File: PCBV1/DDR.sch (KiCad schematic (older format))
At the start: 24 parts, among them U2 MT41K128M16JT-125_K

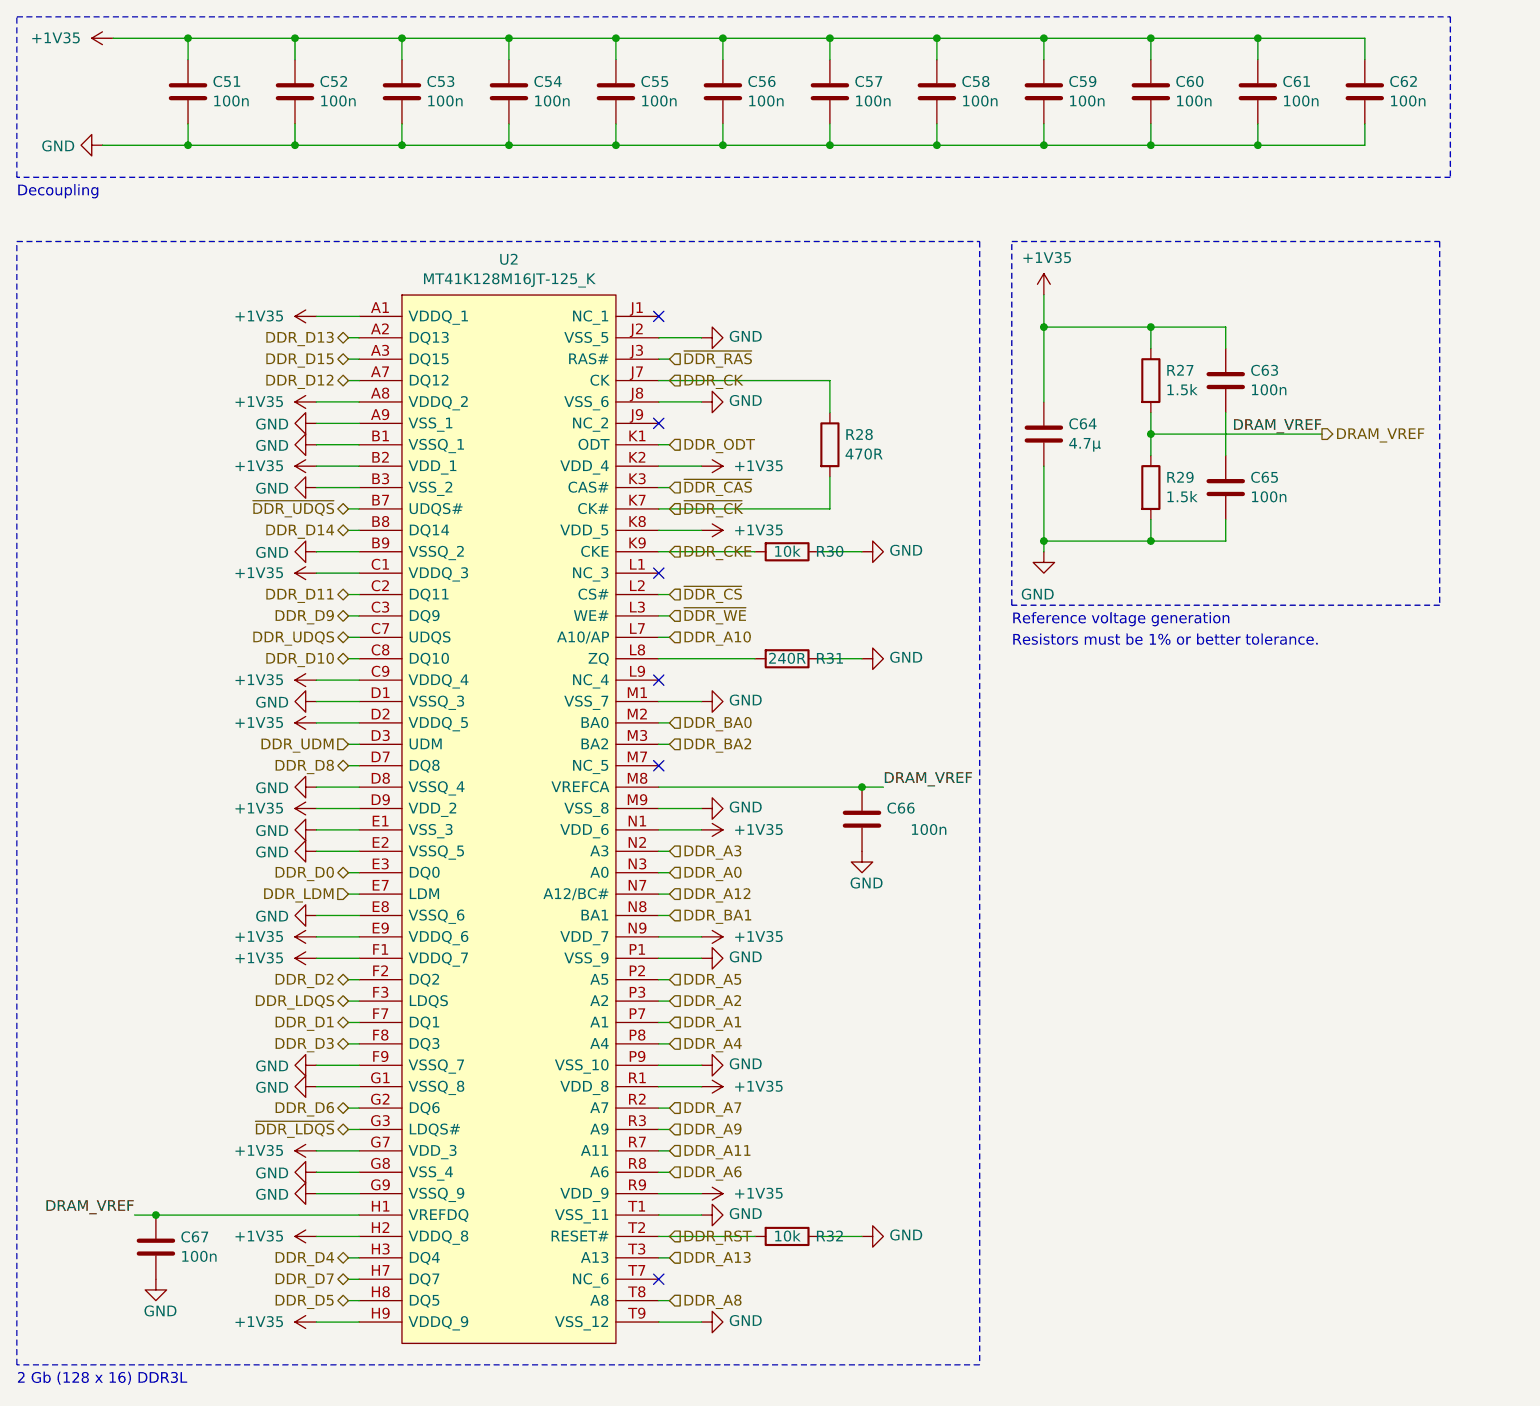
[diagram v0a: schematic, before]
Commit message: Many changes to footprints (0603 -> 0402), basic DDR layout set, no traces made.
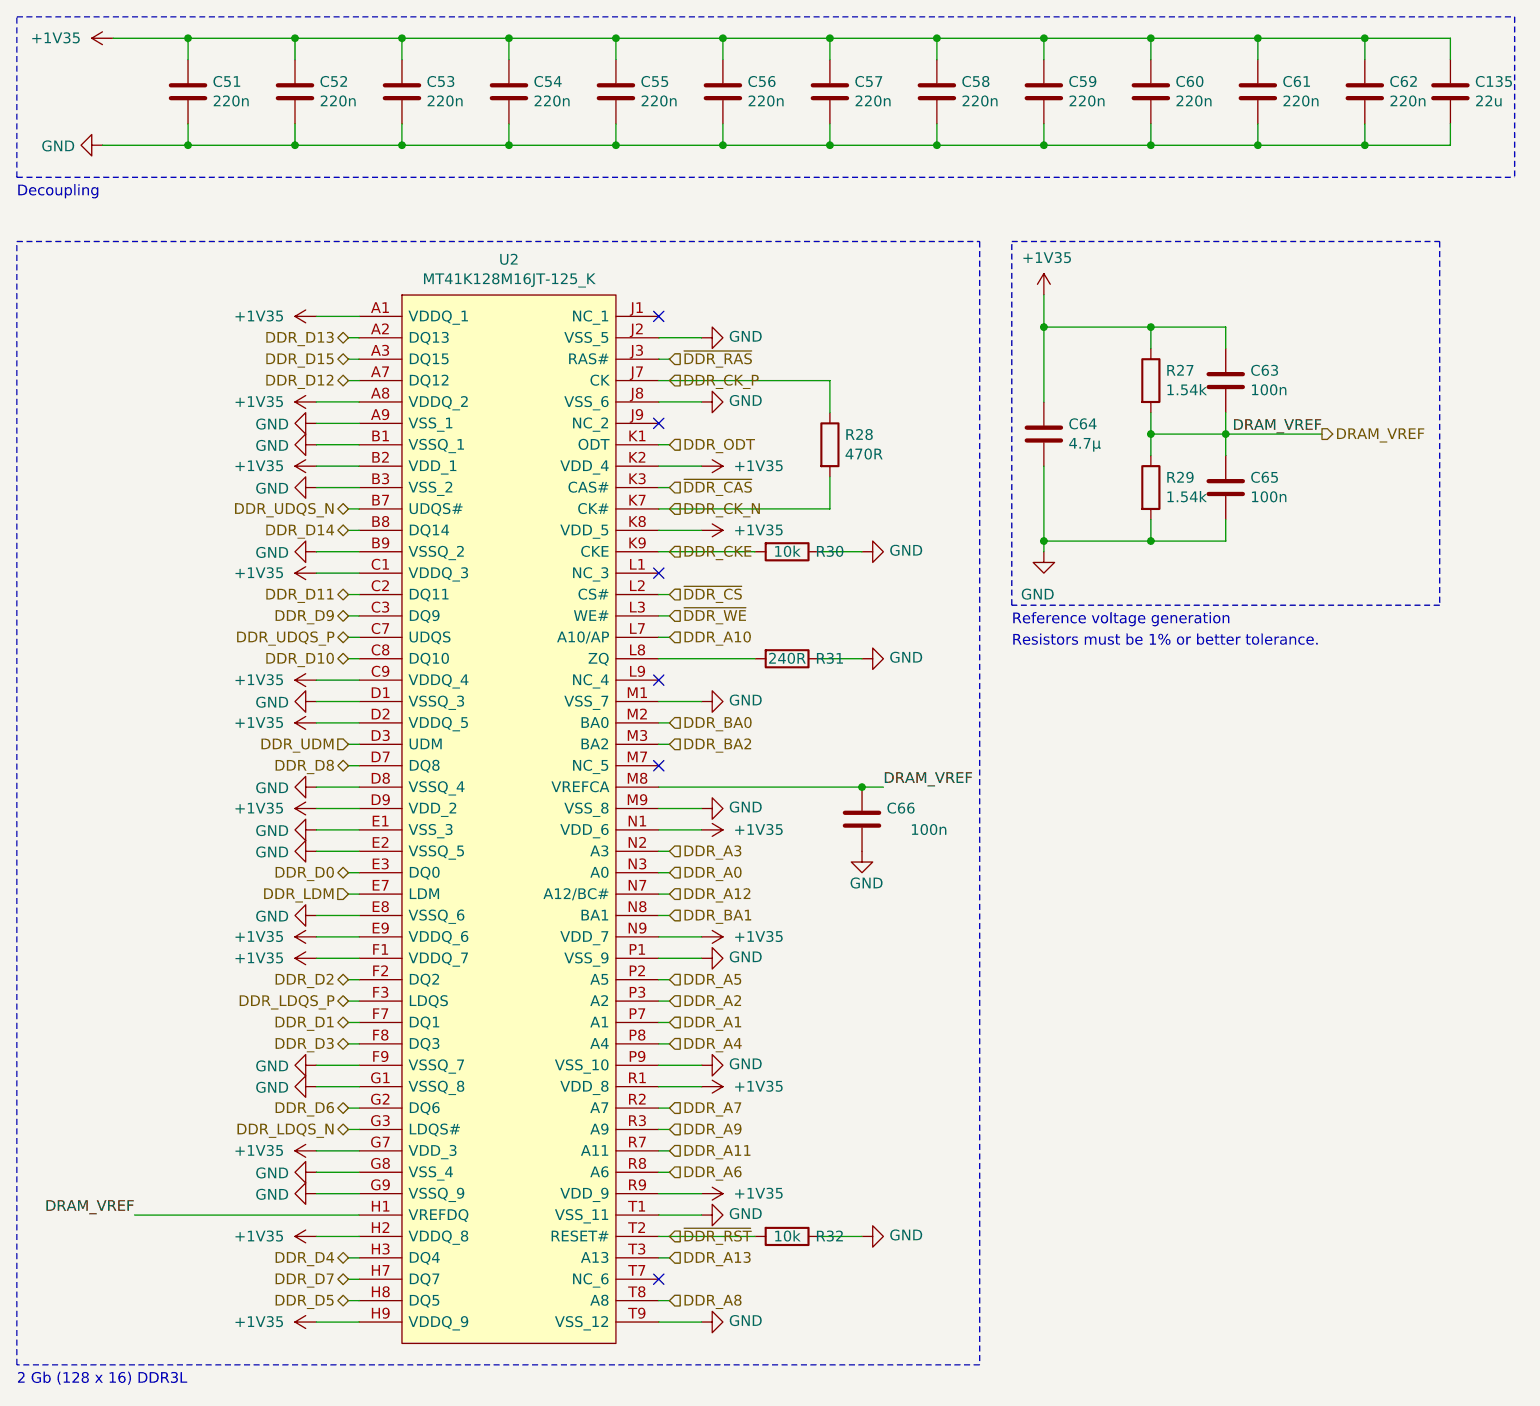
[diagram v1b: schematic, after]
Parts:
- removed C67: 100n, Capacitor_SMD:C_0603_1608Metric, symbol Device:C
- added C135: 22u, Capacitor_SMD:C_0603_1608Metric, symbol Device:C
- C51, C52, C53, C54, C55, C56, C57, C58, C59, C60, C61, C62: value 100n -> 220n; footprint Capacitor_SMD:C_0603_1608Metric -> Capacitor_SMD:C_0402_1005Metric
- C63, C65, C66: footprint Capacitor_SMD:C_0603_1608Metric -> Capacitor_SMD:C_0402_1005Metric
- R27, R29: value 1.5k -> 1.54k; footprint Resistor_SMD:R_0603_1608Metric -> Resistor_SMD:R_0402_1005Metric
- R28, R30, R31, R32: footprint Resistor_SMD:R_0603_1608Metric -> Resistor_SMD:R_0402_1005Metric
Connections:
- net +1V35: now also C135.1
- net DRAM_VREF: now also C63.2, C65.1
- net GND: now also C135.2
- net DDR_CK renamed DDR_CK_P
- net DDR_LDQS renamed DDR_LDQS_P
- net DDR_RST renamed ~DDR_RST
- net DDR_UDQS renamed DDR_UDQS_P
- net ~DDR_CK renamed DDR_CK_N
- net ~DDR_LDQS renamed DDR_LDQS_N
- net ~DDR_UDQS renamed DDR_UDQS_N
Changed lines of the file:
@@
 F 0 "R31" V 4150 3800 50  0000 C CNN
 F 1 "240R" V 4150 3600 50  0000 C CNN
-F 2 "Resistor_SMD:R_0603_1608Metric" V 4080 3600 50  0001 C CNN
+F 2 "Resistor_SMD:R_0402_1005Metric" V 4080 3600 50  0001 C CNN
 F 3 "~" H 4150 3600 50  0001 C CNN
 	1    4150 3600
@@
 DDR_CKE
 Text HLabel 3600 2900 2    50   Input ~ 0
-~DDR_CK
+DDR_CK_N
 Text HLabel 3600 2800 2    50   Input ~ 0
 ~DDR_CAS
@@
 	3550 2800 3600 2800
 Text HLabel 3600 2300 2    50   Input ~ 0
-DDR_CK
+DDR_CK_P
 Text HLabel 3600 2200 2    50   Input ~ 0
 ~DDR_RAS
@@
 	3550 2200 3600 2200
 Text HLabel 2100 2900 0    50   BiDi ~ 0
-~DDR_UDQS
+DDR_UDQS_N
 Wire Wire Line
 	2100 2900 2150 2900
 Text HLabel 2100 3500 0    50   BiDi ~ 0
-DDR_UDQS
+DDR_UDQS_P
 Wire Wire Line
 	2100 3500 2150 3500
@@
 	2100 4700 2150 4700
 Text HLabel 2100 5200 0    50   BiDi ~ 0
-DDR_LDQS
+DDR_LDQS_P
 Wire Wire Line
 	2100 5200 2150 5200
 Text HLabel 2100 5800 0    50   BiDi ~ 0
-~DDR_LDQS
+DDR_LDQS_N
 Wire Wire Line
 	2100 5800 2150 5800
@@
 	3750 6100 3550 6100
 Text HLabel 3600 6300 2    50   Input ~ 0
-DDR_RST
+~DDR_RST
 $Comp
 L power:+1V35 #PWR0120
@@
 P 1350 950
 F 0 "C51" H 1465 996 50  0000 L CNN
-F 1 "100n" H 1465 905 50  0000 L CNN
-F 2 "Capacitor_SMD:C_0603_1608Metric" H 1388 800 50  0001 C CNN
+F 1 "220n" H 1465 905 50  0000 L CNN
+F 2 "Capacitor_SMD:C_0402_1005Metric" H 1388 800 50  0001 C CNN
 F 3 "~" H 1350 950 50  0001 C CNN
 	1    1350 950
@@
 P 1850 950
 F 0 "C52" H 1965 996 50  0000 L CNN
-F 1 "100n" H 1965 905 50  0000 L CNN
-F 2 "Capacitor_SMD:C_0603_1608Metric" H 1888 800 50  0001 C CNN
+F 1 "220n" H 1965 905 50  0000 L CNN
+F 2 "Capacitor_SMD:C_0402_1005Metric" H 1888 800 50  0001 C CNN
 F 3 "~" H 1850 950 50  0001 C CNN
 	1    1850 950
@@
 P 2350 950
 F 0 "C53" H 2465 996 50  0000 L CNN
-F 1 "100n" H 2465 905 50  0000 L CNN
-F 2 "Capacitor_SMD:C_0603_1608Metric" H 2388 800 50  0001 C CNN
+F 1 "220n" H 2465 905 50  0000 L CNN
+F 2 "Capacitor_SMD:C_0402_1005Metric" H 2388 800 50  0001 C CNN
 F 3 "~" H 2350 950 50  0001 C CNN
 	1    2350 950
@@
 P 2850 950
 F 0 "C54" H 2965 996 50  0000 L CNN
-F 1 "100n" H 2965 905 50  0000 L CNN
-F 2 "Capacitor_SMD:C_0603_1608Metric" H 2888 800 50  0001 C CNN
+F 1 "220n" H 2965 905 50  0000 L CNN
+F 2 "Capacitor_SMD:C_0402_1005Metric" H 2888 800 50  0001 C CNN
 F 3 "~" H 2850 950 50  0001 C CNN
 	1    2850 950
@@
 P 3350 950
 F 0 "C55" H 3465 996 50  0000 L CNN
-F 1 "100n" H 3465 905 50  0000 L CNN
-F 2 "Capacitor_SMD:C_0603_1608Metric" H 3388 800 50  0001 C CNN
+F 1 "220n" H 3465 905 50  0000 L CNN
+F 2 "Capacitor_SMD:C_0402_1005Metric" H 3388 800 50  0001 C CNN
 F 3 "~" H 3350 950 50  0001 C CNN
 	1    3350 950
@@
 P 3850 950
 F 0 "C56" H 3965 996 50  0000 L CNN
-F 1 "100n" H 3965 905 50  0000 L CNN
-F 2 "Capacitor_SMD:C_0603_1608Metric" H 3888 800 50  0001 C CNN
+F 1 "220n" H 3965 905 50  0000 L CNN
+F 2 "Capacitor_SMD:C_0402_1005Metric" H 3888 800 50  0001 C CNN
 F 3 "~" H 3850 950 50  0001 C CNN
 	1    3850 950
@@
 P 4350 950
 F 0 "C57" H 4465 996 50  0000 L CNN
-F 1 "100n" H 4465 905 50  0000 L CNN
-F 2 "Capacitor_SMD:C_0603_1608Metric" H 4388 800 50  0001 C CNN
+F 1 "220n" H 4465 905 50  0000 L CNN
+F 2 "Capacitor_SMD:C_0402_1005Metric" H 4388 800 50  0001 C CNN
 F 3 "~" H 4350 950 50  0001 C CNN
 	1    4350 950
@@
 P 4850 950
 F 0 "C58" H 4965 996 50  0000 L CNN
-F 1 "100n" H 4965 905 50  0000 L CNN
-F 2 "Capacitor_SMD:C_0603_1608Metric" H 4888 800 50  0001 C CNN
+F 1 "220n" H 4965 905 50  0000 L CNN
+F 2 "Capacitor_SMD:C_0402_1005Metric" H 4888 800 50  0001 C CNN
 F 3 "~" H 4850 950 50  0001 C CNN
 	1    4850 950
@@
 P 5350 950
 F 0 "C59" H 5465 996 50  0000 L CNN
-F 1 "100n" H 5465 905 50  0000 L CNN
-F 2 "Capacitor_SMD:C_0603_1608Metric" H 5388 800 50  0001 C CNN
+F 1 "220n" H 5465 905 50  0000 L CNN
+F 2 "Capacitor_SMD:C_0402_1005Metric" H 5388 800 50  0001 C CNN
 F 3 "~" H 5350 950 50  0001 C CNN
 	1    5350 950
@@
 P 5850 950
 F 0 "C60" H 5965 996 50  0000 L CNN
-F 1 "100n" H 5965 905 50  0000 L CNN
-F 2 "Capacitor_SMD:C_0603_1608Metric" H 5888 800 50  0001 C CNN
+F 1 "220n" H 5965 905 50  0000 L CNN
+F 2 "Capacitor_SMD:C_0402_1005Metric" H 5888 800 50  0001 C CNN
 F 3 "~" H 5850 950 50  0001 C CNN
 	1    5850 950
@@
 P 6350 950
 F 0 "C61" H 6465 996 50  0000 L CNN
-F 1 "100n" H 6465 905 50  0000 L CNN
-F 2 "Capacitor_SMD:C_0603_1608Metric" H 6388 800 50  0001 C CNN
+F 1 "220n" H 6465 905 50  0000 L CNN
+F 2 "Capacitor_SMD:C_0402_1005Metric" H 6388 800 50  0001 C CNN
 F 3 "~" H 6350 950 50  0001 C CNN
 	1    6350 950
@@
 P 6850 950
 F 0 "C62" H 6965 996 50  0000 L CNN
-F 1 "100n" H 6965 905 50  0000 L CNN
-F 2 "Capacitor_SMD:C_0603_1608Metric" H 6888 800 50  0001 C CNN
+F 1 "220n" H 6965 905 50  0000 L CNN
+F 2 "Capacitor_SMD:C_0402_1005Metric" H 6888 800 50  0001 C CNN
 F 3 "~" H 6850 950 50  0001 C CNN
 	1    6850 950
@@
 P 5850 2300
 F 0 "R27" H 5920 2346 50  0000 L CNN
-F 1 "1.5k" H 5920 2255 50  0000 L CNN
-F 2 "Resistor_SMD:R_0603_1608Metric" V 5780 2300 50  0001 C CNN
+F 1 "1.54k" H 5920 2255 50  0000 L CNN
+F 2 "Resistor_SMD:R_0402_1005Metric" V 5780 2300 50  0001 C CNN
 F 3 "~" H 5850 2300 50  0001 C CNN
 	1    5850 2300
@@
 P 5850 2800
 F 0 "R29" H 5920 2846 50  0000 L CNN
-F 1 "1.5k" H 5920 2755 50  0000 L CNN
-F 2 "Resistor_SMD:R_0603_1608Metric" V 5780 2800 50  0001 C CNN
+F 1 "1.54k" H 5920 2755 50  0000 L CNN
+F 2 "Resistor_SMD:R_0402_1005Metric" V 5780 2800 50  0001 C CNN
 F 3 "~" H 5850 2800 50  0001 C CNN
 	1    5850 2800
@@
 F 0 "C63" H 6315 2346 50  0000 L CNN
 F 1 "100n" H 6315 2255 50  0000 L CNN
-F 2 "Capacitor_SMD:C_0603_1608Metric" H 6238 2150 50  0001 C CNN
+F 2 "Capacitor_SMD:C_0402_1005Metric" H 6238 2150 50  0001 C CNN
 F 3 "~" H 6200 2300 50  0001 C CNN
 	1    6200 2300
@@
 F 0 "C65" H 6315 2846 50  0000 L CNN
 F 1 "100n" H 6315 2755 50  0000 L CNN
-F 2 "Capacitor_SMD:C_0603_1608Metric" H 6238 2650 50  0001 C CNN
+F 2 "Capacitor_SMD:C_0402_1005Metric" H 6238 2650 50  0001 C CNN
 F 3 "~" H 6200 2800 50  0001 C CNN
 	1    6200 2800
@@
 Connection ~ 5850 2050
 Wire Wire Line
-	6200 2450 6200 2650
-Wire Wire Line
-	5850 2450 5850 2550
-Connection ~ 5850 2550
-Wire Wire Line
-	5850 2550 5850 2650
+	6200 2450 6200 2550
 Text Label 6650 2550 2    50   ~ 0
 DRAM_VREF
-Wire Wire Line
-	5850 2550 6650 2550
 Text HLabel 6650 2550 2    50   Output ~ 0
 DRAM_VREF
@@
 Text Label 1100 6200 2    50   ~ 0
 DRAM_VREF
-$Comp
-L Device:C C67
-U 1 1 6049FFC4
-P 1200 6350
-F 0 "C67" H 1315 6396 50  0000 L CNN
-F 1 "100n" H 1315 6305 50  0000 L CNN
-F 2 "Capacitor_SMD:C_0603_1608Metric" H 1238 6200 50  0001 C CNN
-F 3 "~" H 1200 6350 50  0001 C CNN
-	1    1200 6350
-	1    0    0    -1
-$EndComp
-Wire Wire Line
-	1100 6200 1200 6200
-Connection ~ 1200 6200
-Wire Wire Line
-	1200 6200 2150 6200
 Text Label 4600 4200 0    50   ~ 0
 DRAM_VREF
@@
 F 0 "C66" H 4250 4300 50  0000 L CNN
 F 1 "100n" H 4100 4400 50  0000 L CNN
-F 2 "Capacitor_SMD:C_0603_1608Metric" H 4538 4200 50  0001 C CNN
+F 2 "Capacitor_SMD:C_0402_1005Metric" H 4538 4200 50  0001 C CNN
 F 3 "~" H 4500 4350 50  0001 C CNN
 	1    4500 4350
@@
 	1    0    0    -1
 $EndComp
-$Comp
-L power:GND #PWR0128
-U 1 1 604B3DEB
-P 1200 6500
-F 0 "#PWR0128" H 1200 6250 50  0001 C CNN
-F 1 "GND" H 1300 6350 50  0000 R CNN
-F 2 "" H 1200 6500 50  0001 C CNN
-F 3 "" H 1200 6500 50  0001 C CNN
-	1    1200 6500
-	1    0    0    -1
-$EndComp
 Wire Notes Line
 	550  6900 550  1650
@@
 Text Notes 550  7000 0    50   ~ 0
 2 Gb (128 x 16) DDR3L
-Wire Notes Line
-	550  600  7250 600
-Wire Notes Line
-	7250 600  7250 1350
-Wire Notes Line
-	7250 1350 550  1350
 Wire Notes Line
 	550  1350 550  600
@@
 F 0 "R32" V 4150 6500 50  0000 C CNN
 F 1 "10k" V 4150 6300 50  0000 C CNN
-F 2 "Resistor_SMD:R_0603_1608Metric" V 4080 6300 50  0001 C CNN
+F 2 "Resistor_SMD:R_0402_1005Metric" V 4080 6300 50  0001 C CNN
 F 3 "~" H 4150 6300 50  0001 C CNN
 	1    4150 6300
@@
 F 0 "R30" V 4150 3300 50  0000 C CNN
 F 1 "10k" V 4150 3100 50  0000 C CNN
-F 2 "Resistor_SMD:R_0603_1608Metric" V 4080 3100 50  0001 C CNN
+F 2 "Resistor_SMD:R_0402_1005Metric" V 4080 3100 50  0001 C CNN
 F 3 "~" H 4150 3100 50  0001 C CNN
 	1    4150 3100
@@
 F 0 "R28" H 4420 2646 50  0000 L CNN
 F 1 "470R" H 4420 2555 50  0000 L CNN
-F 2 "Resistor_SMD:R_0603_1608Metric" V 4280 2600 50  0001 C CNN
+F 2 "Resistor_SMD:R_0402_1005Metric" V 4280 2600 50  0001 C CNN
 F 3 "~" H 4350 2600 50  0001 C CNN
 	1    4350 2600
@@
 Wire Wire Line
 	4350 2750 4350 2900
+Wire Wire Line
+	5850 2450 5850 2550
+Wire Wire Line
+	5850 2550 6200 2550
+Connection ~ 5850 2550
+Wire Wire Line
+	5850 2550 5850 2650
+Connection ~ 6200 2550
+Wire Wire Line
+	6200 2550 6200 2650
+Wire Wire Line
+	6200 2550 6650 2550
+$Comp
+L Device:C C135
+U 1 1 628AE7E6
+P 7250 950
+F 0 "C135" H 7365 996 50  0000 L CNN
+F 1 "22u" H 7365 905 50  0000 L CNN
+F 2 "Capacitor_SMD:C_0603_1608Metric" H 7288 800 50  0001 C CNN
+F 3 "~" H 7250 950 50  0001 C CNN
+	1    7250 950
+	1    0    0    -1
+$EndComp
+Wire Notes Line
+	7550 600  7550 1350
+Wire Notes Line
+	550  600  7550 600
+Wire Notes Line
+	550  1350 7550 1350
+Wire Wire Line
+	7250 1100 7250 1200
+Wire Wire Line
+	7250 1200 6850 1200
+Connection ~ 6850 1200
+Wire Wire Line
+	6850 700  7250 700
+Wire Wire Line
+	7250 700  7250 800
+Connection ~ 6850 700
+Wire Wire Line
+	1100 6200 2150 6200
 $EndSCHEMATC
